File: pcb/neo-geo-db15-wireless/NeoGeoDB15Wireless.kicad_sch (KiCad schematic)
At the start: 5 parts, among them J1 DB15_F, U1 RP2040-Zero, U2 NRF24L01_Breakout

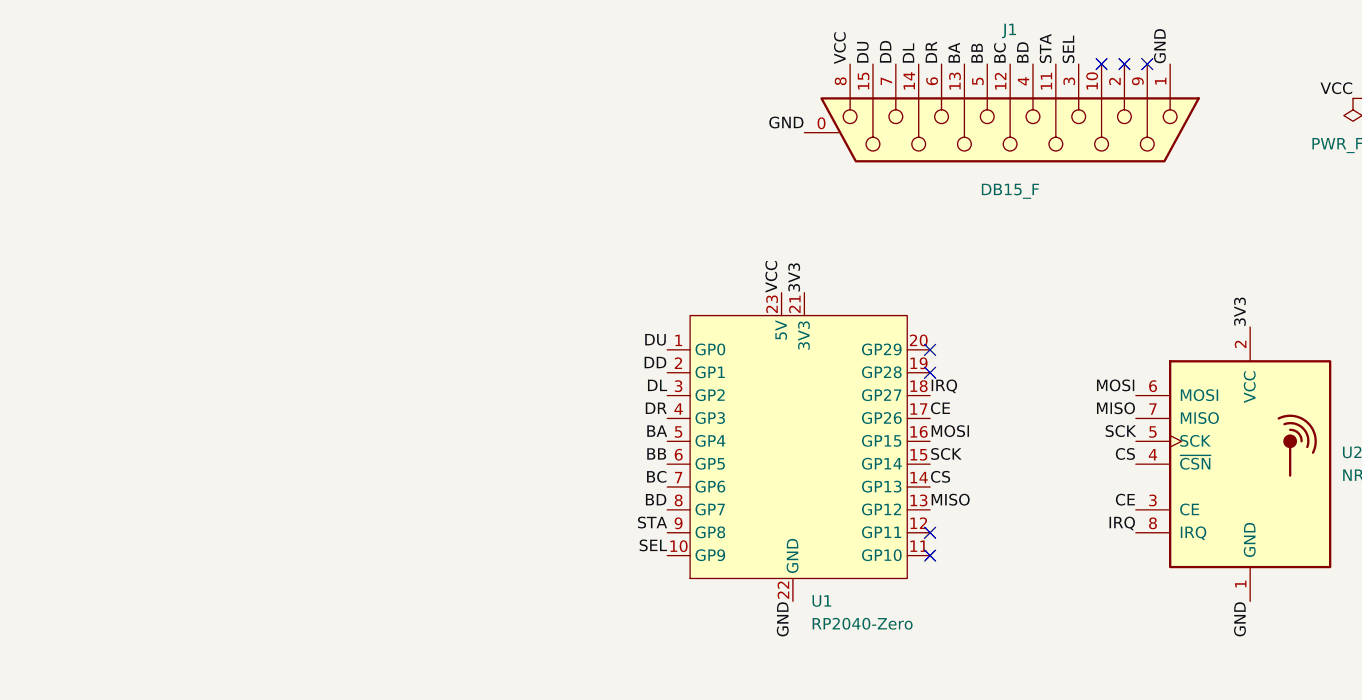
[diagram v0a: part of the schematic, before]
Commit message: Adds resistor packs for current limiting on button lines
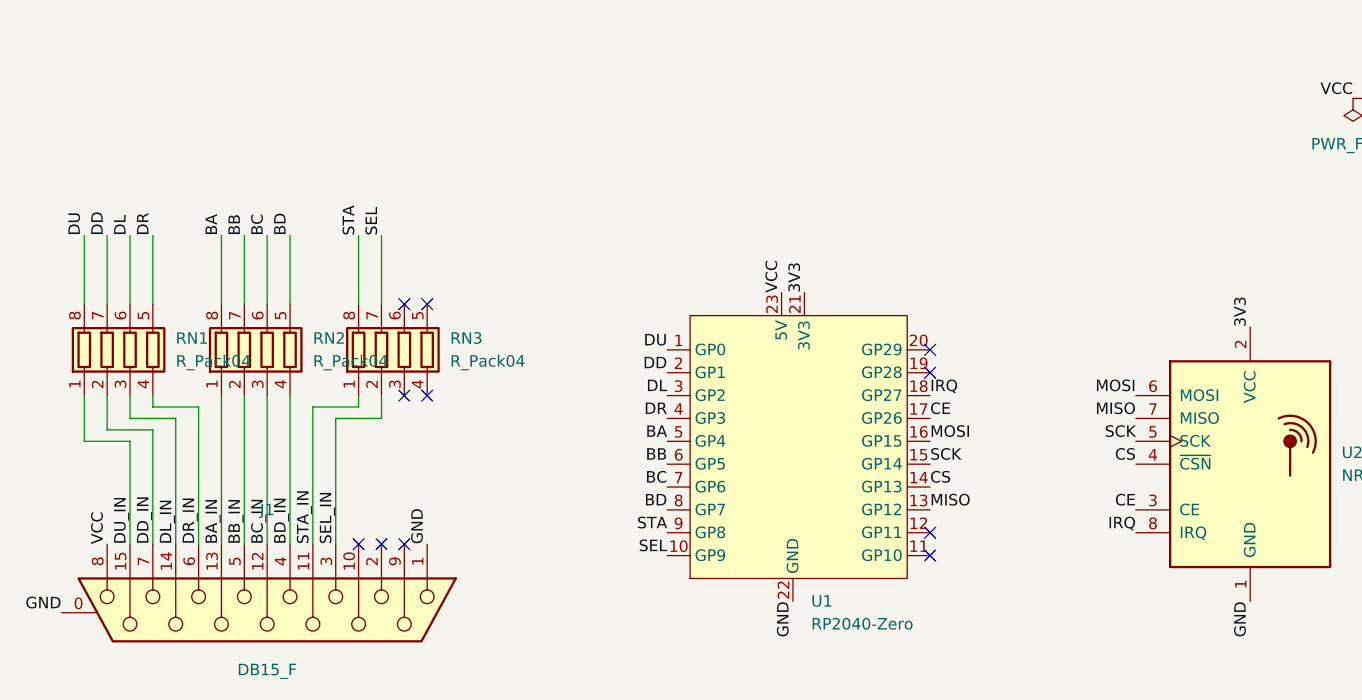
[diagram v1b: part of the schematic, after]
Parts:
- added RN1, RN2, RN3: R_Pack04, Resistor_SMD:R_Array_Convex_4x1206, symbol Device:R_Pack04
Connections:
- net BA: now also RN2.8 (R1.2); no longer J1.13 (P13)
- net BB: now also RN2.7 (R2.2); no longer J1.5
- net BC: now also RN2.6 (R3.2); no longer J1.12 (P12)
- net BD: now also RN2.5 (R4.2); no longer J1.4
- net DD: now also RN1.7 (R2.2); no longer J1.7
- net DL: now also RN1.6 (R3.2); no longer J1.14 (P14)
- net DR: now also RN1.5 (R4.2); no longer J1.6
- net DU: now also RN1.8 (R1.2); no longer J1.15 (P15)
- net SEL: now also RN3.7 (R2.2); no longer J1.3
- net STA: now also RN3.8 (R1.2); no longer J1.11 (P111)
- new net BA_IN: J1.13 (P13), RN2.1 (R1.1)
- new net BB_IN: J1.5, RN2.2 (R2.1)
- new net BC_IN: J1.12 (P12), RN2.3 (R3.1)
- new net BD_IN: J1.4, RN2.4 (R4.1)
- new net DD_IN: J1.7, RN1.2 (R2.1)
- new net DL_IN: J1.14 (P14), RN1.3 (R3.1)
- new net DR_IN: J1.6, RN1.4 (R4.1)
- new net DU_IN: J1.15 (P15), RN1.1 (R1.1)
- new net SEL_IN: J1.3, RN3.2 (R2.1)
- new net STA_IN: J1.11 (P111), RN3.1 (R1.1)
- no-connect marks 7 -> 11
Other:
- moved on the sheet: J1

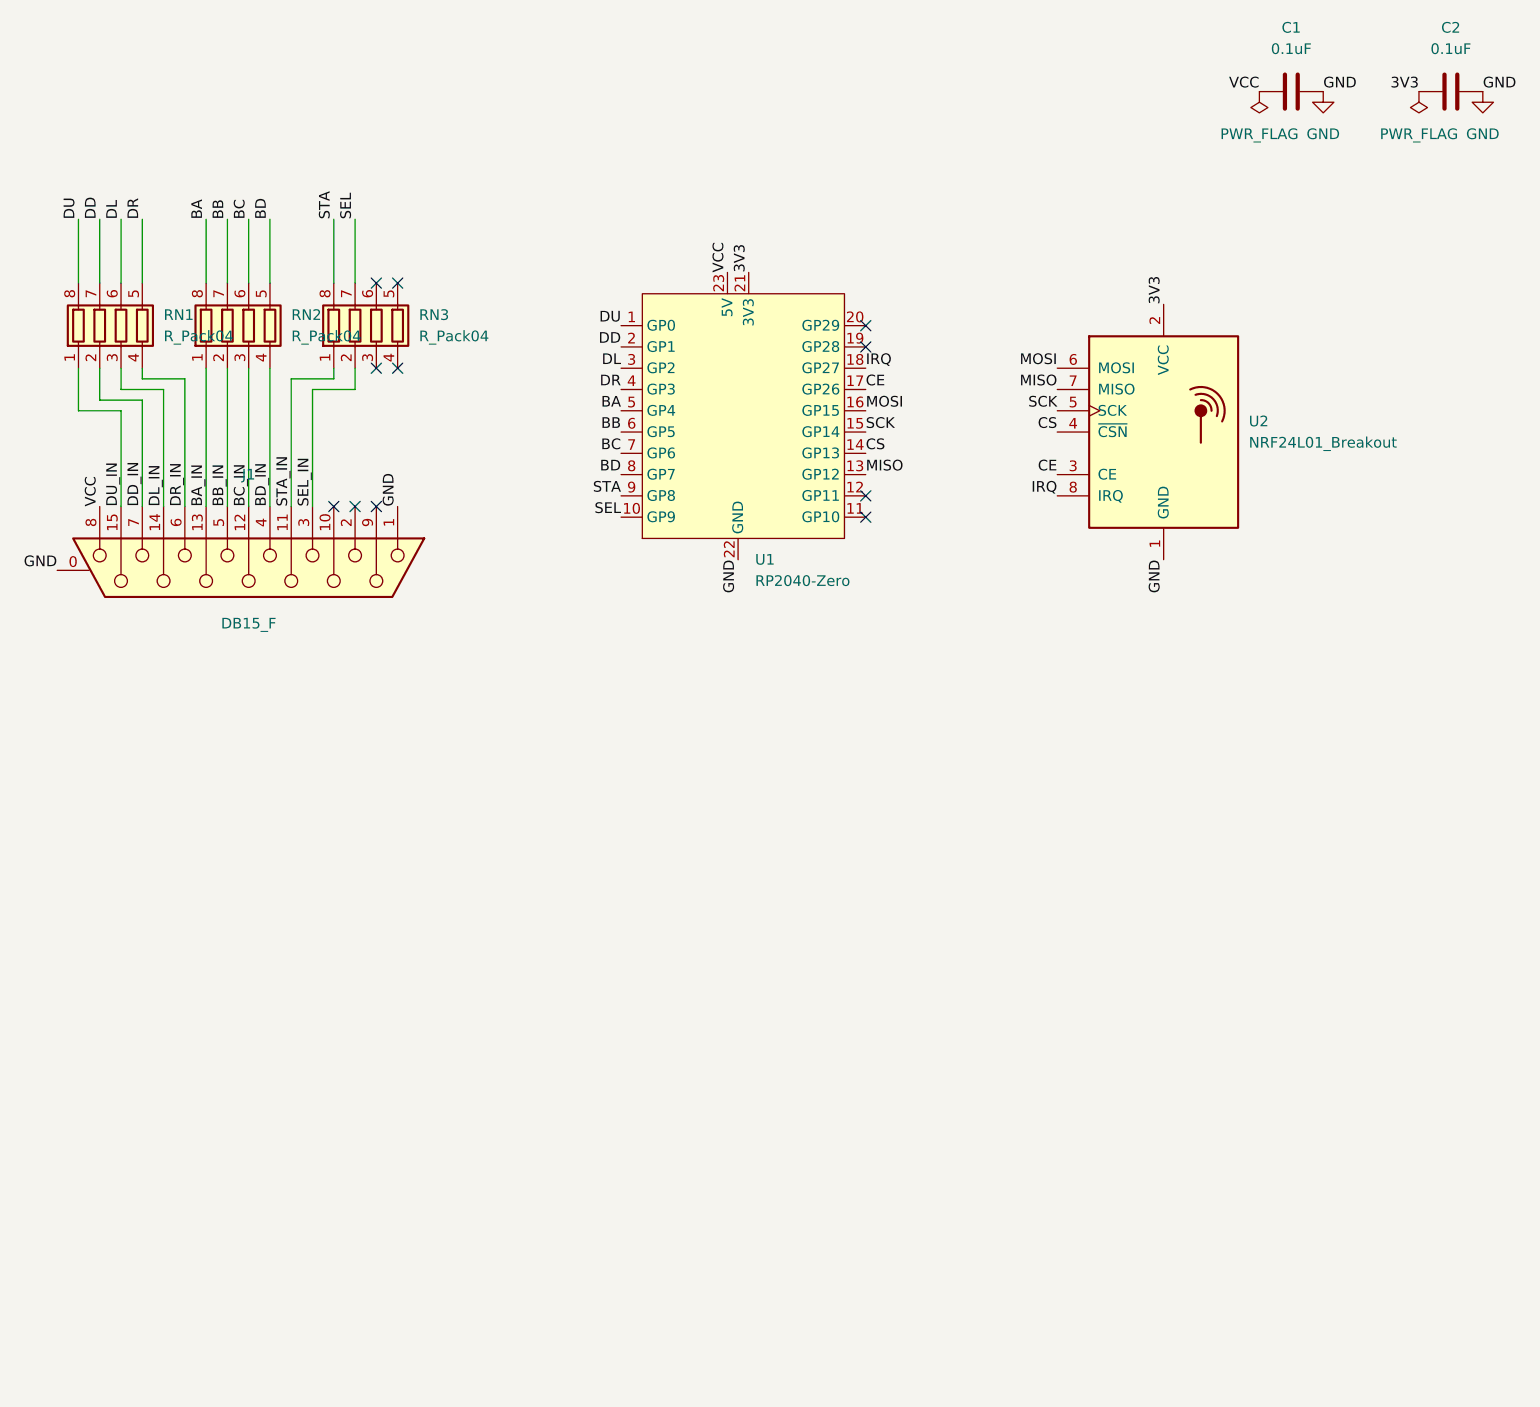
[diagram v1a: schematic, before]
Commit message: Voltage dividers on button inputs for pico safety
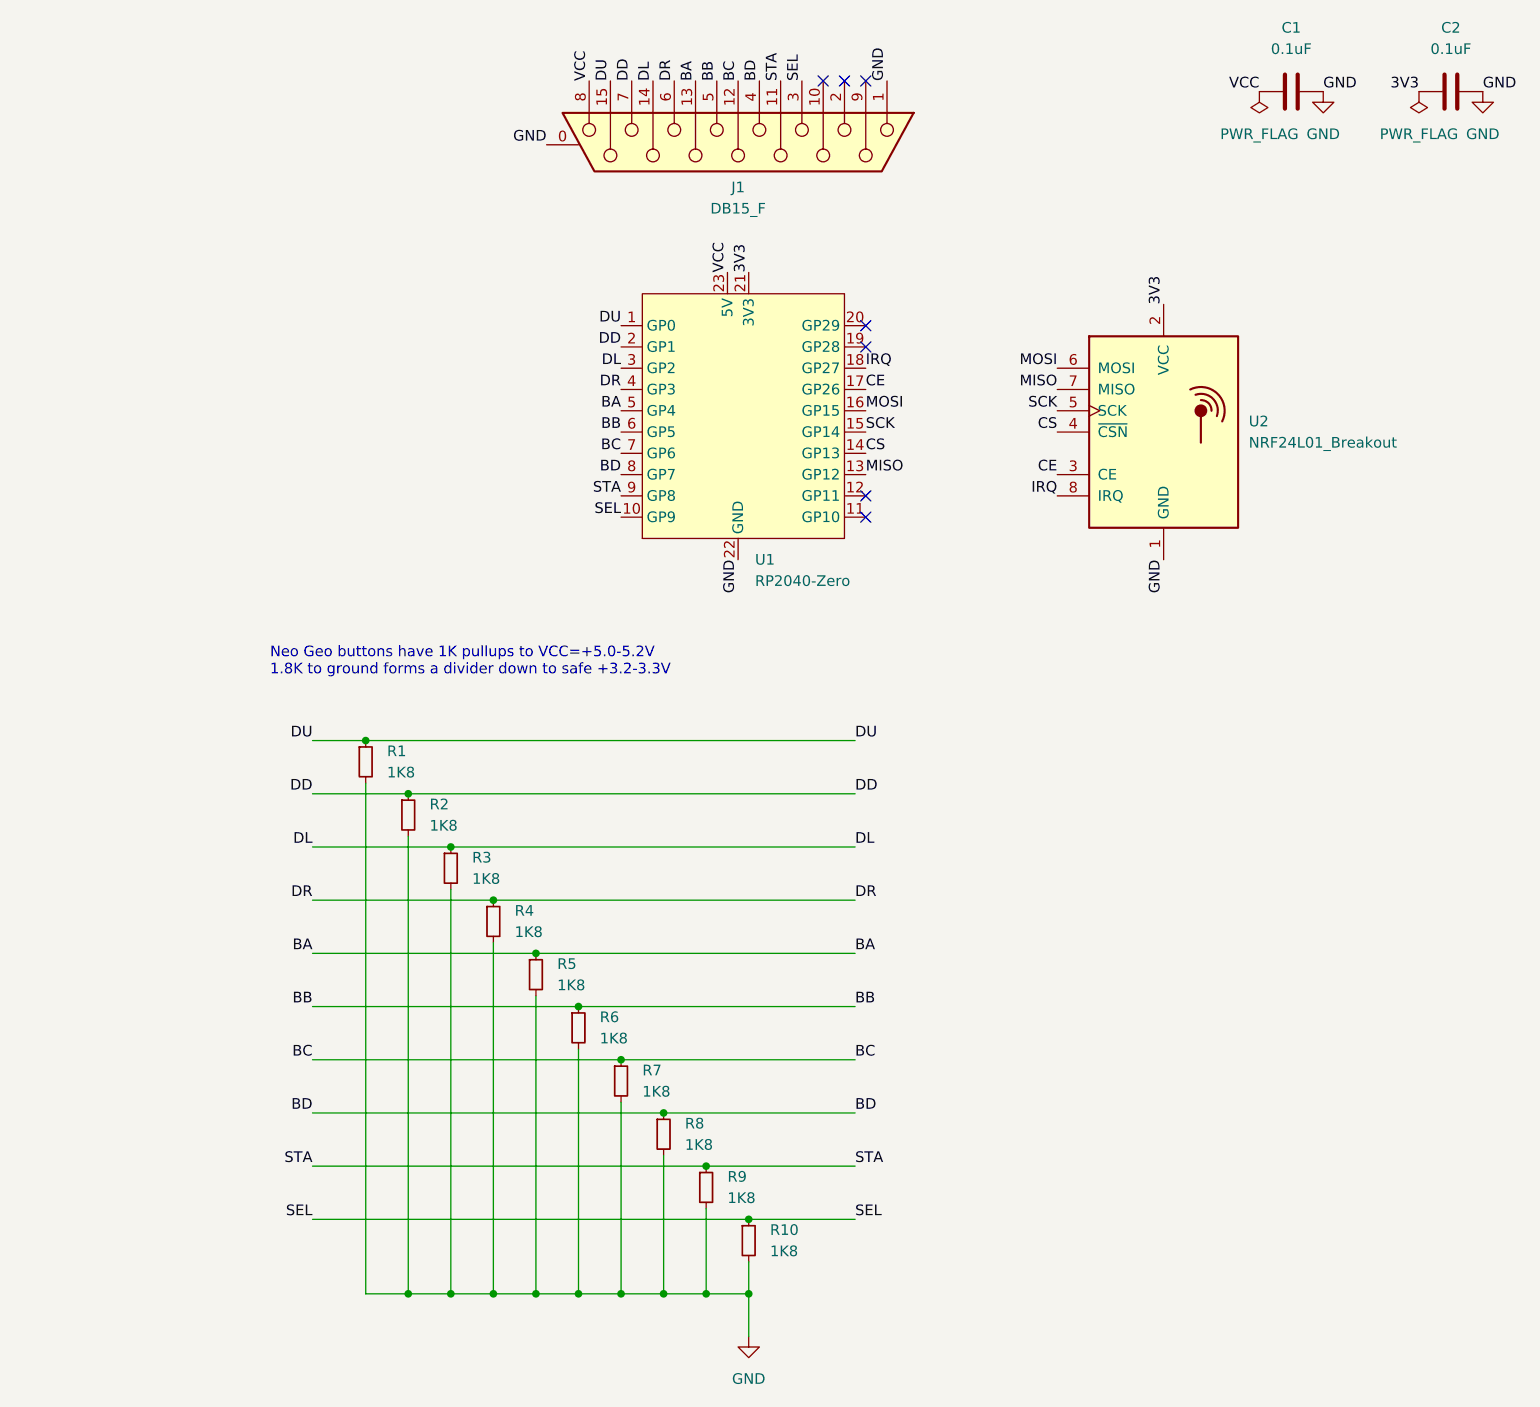
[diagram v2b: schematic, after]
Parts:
- removed RN1, RN2, RN3: R_Pack04, Resistor_SMD:R_Array_Convex_4x1206, symbol Device:R_Pack04
- added R1, R10, R2, R3, R4, R5, R6, R7, R8, R9: 1K8, Resistor_SMD:R_0805_2012Metric_Pad1.20x1.40mm_HandSolder, symbol Device:R_Small
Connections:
- net BA_IN is gone; now on net BA: J1.13 (P13)
- net BB_IN is gone; now on net BB: J1.5
- net BC_IN is gone; now on net BC: J1.12 (P12)
- net BD_IN is gone; now on net BD: J1.4
- net DD_IN is gone; now on net DD: J1.7
- net DL_IN is gone; now on net DL: J1.14 (P14)
- net DR_IN is gone; now on net DR: J1.6
- net DU_IN is gone; now on net DU: J1.15 (P15)
- net SEL_IN is gone; now on net SEL: J1.3
- net STA_IN is gone; now on net STA: J1.11 (P111)
- net BA: now also R5.1
- net BB: now also R6.1
- net BC: now also R7.1
- net BD: now also R8.1
- net DD: now also R2.1
- net DL: now also R3.1
- net DR: now also R4.1
- net DU: now also R1.1
- net GND: now also R1.2, R10.2, R2.2, R3.2, R4.2, R5.2, R6.2, R7.2, R8.2, R9.2
- net SEL: now also R10.1
- net STA: now also R9.1
- no-connect marks 11 -> 7
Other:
- note added: "Neo Geo buttons have 1K pullups to VCC=+5.0-5.2V 1.8K to ground forms a divider down to safe +3.2-3.3V"
- moved on the sheet: J1

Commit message: Use 0805 capacitors
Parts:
- C1, C2: footprint Capacitor_SMD:C_0603_1608Metric_Pad1.08x0.95mm_HandSolder -> Capacitor_SMD:C_0805_2012Metric_Pad1.18x1.45mm_HandSolder
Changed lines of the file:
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@@
       (effects (font (size 1.27 1.27)))
     )
-    (property "Footprint" "Capacitor_SMD:C_0603_1608Metric_Pad1.08x0.95mm_HandSolder" (at 185.42 26.9748 0)
+    (property "Footprint" "Capacitor_SMD:C_0805_2012Metric_Pad1.18x1.45mm_HandSolder" (at 185.42 26.9748 0)
       (effects (font (size 1.27 1.27)) hide)
     )
@@
       (effects (font (size 1.27 1.27)))
     )
-    (property "Footprint" "Capacitor_SMD:C_0603_1608Metric_Pad1.08x0.95mm_HandSolder" (at 204.47 26.9748 0)
-      (effects (font (size 1.27 1.27)) hide)
-    )
+    (property "Footprint" "Capacitor_SMD:C_0805_2012Metric_Pad1.18x1.45mm_HandSolder" (at 204.47 26.9748 0)
+      (effects (font (size 1.27 1.27)) hide)
+    )
